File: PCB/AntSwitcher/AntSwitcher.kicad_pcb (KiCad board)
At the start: 2 copper layers, 33 parts, among them J1 Barrel_Jack, J2 TRX_UKW, J3 TRX2, J4 ANT1, J5 ANT2, K1 HF3-53, K2 HF3-53, K3 HF3-53, K4 HF3-53, Q1 Q_NMOS_GSD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

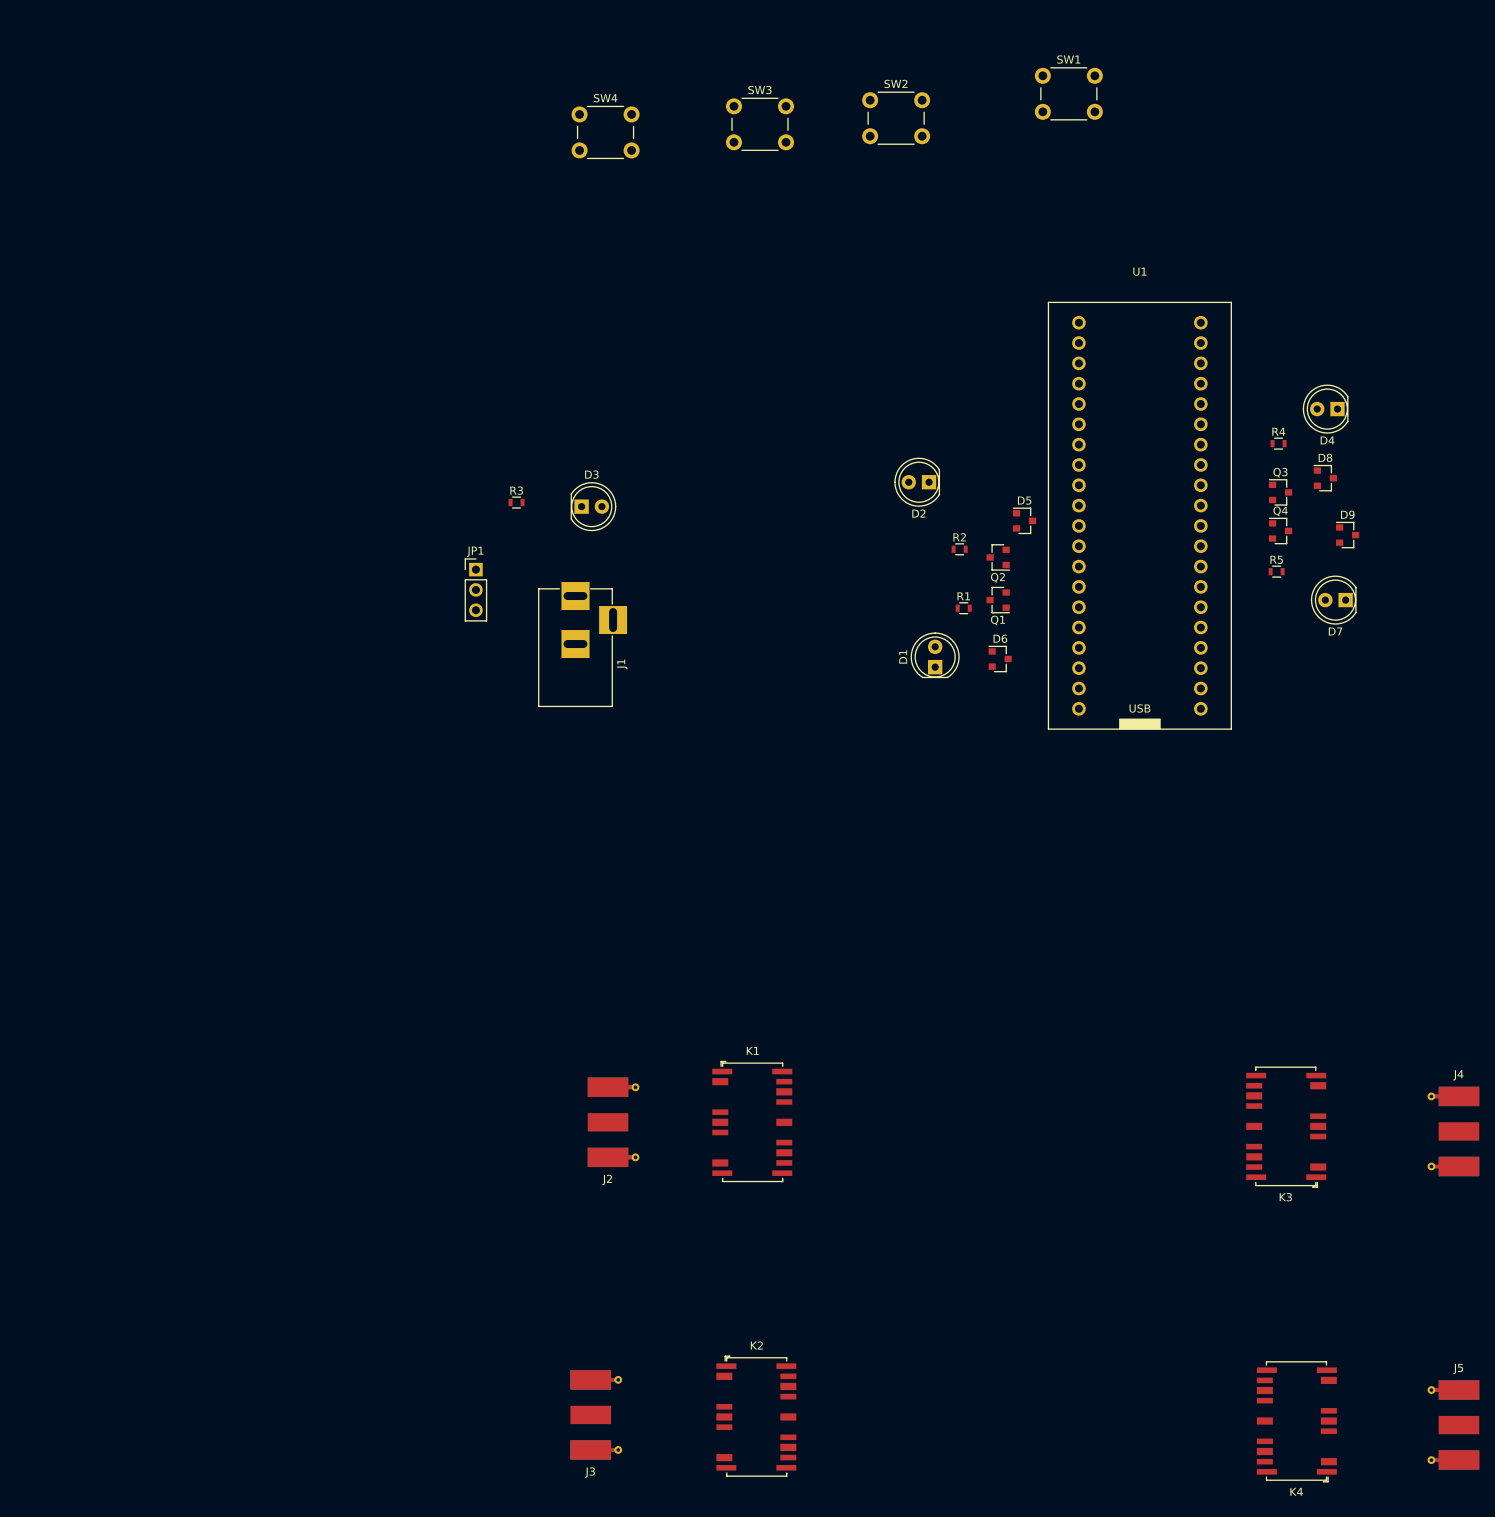
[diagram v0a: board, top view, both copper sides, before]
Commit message: HF-Layout Relays
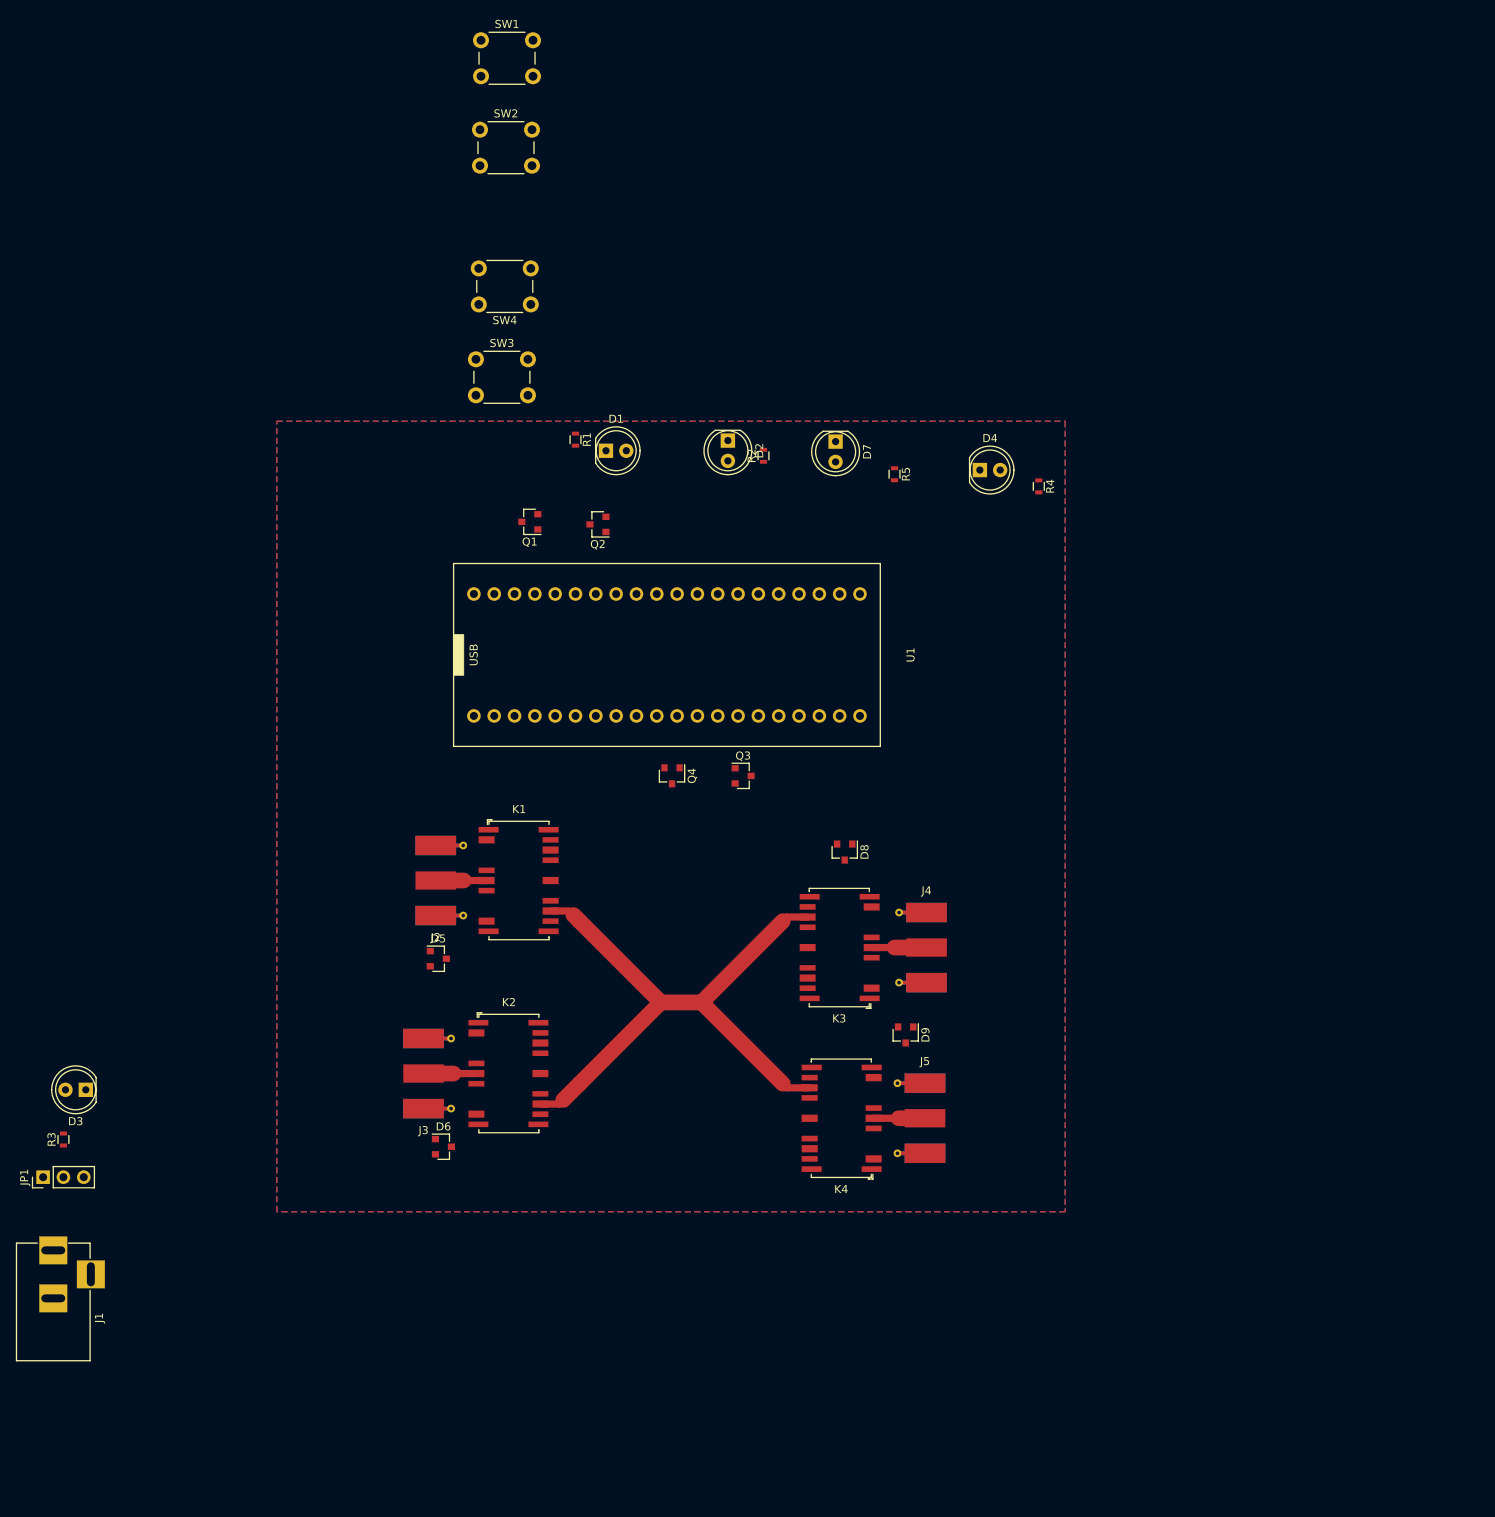
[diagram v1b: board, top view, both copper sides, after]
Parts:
- moved J1 104.6 mm to (36.3, 165.4)
- moved R3 97.7 mm to (37.6, 151.5), turned to 90 degrees
- moved D3 95.7 mm to (40.4, 145.3), turned to 180 degrees
- moved JP1 93.2 mm to (35.1, 156.2), turned to 90 degrees
- moved D6 92.5 mm to (85.1, 152.4)
- moved D5 91.5 mm to (84.5, 128.9)
- moved D9 83.4 mm to (142.9, 138.4), turned to 270 degrees
- moved Q4 82.0 mm to (113.7, 106.0), turned to 270 degrees
- moved J5 77.0 mm to (143.6, 148.8)
- moved D8 76.1 mm to (135.3, 115.6), turned to 270 degrees
- moved Q3 76.0 mm to (122.6, 106.0)
- moved J4 70.4 mm to (143.8, 127.5)
- moved SW1 70.4 mm to (89.8, 14.1)
- moved K4 68.3 mm to (134.9, 148.8)
- moved D7 66.8 mm to (134.1, 64.3), turned to 270 degrees
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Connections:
- D5 pad 1: Net-(D5-Pad1) -> GNDREF
- D5 pad 2: GNDREF -> (no net)
- D5 pad 3: (no net) -> Net-(D5-Pad3)
- D6 pad 1: Net-(D6-Pad1) -> GNDREF
- D6 pad 2: GNDREF -> (no net)
- D6 pad 3: (no net) -> Net-(D6-Pad3)
- D8 pad 1: Net-(D8-Pad1) -> GNDREF
- D8 pad 2: GNDREF -> (no net)
- D8 pad 3: (no net) -> Net-(D8-Pad3)
- D9 pad 1: Net-(D9-Pad1) -> GNDREF
- D9 pad 2: GNDREF -> (no net)
- D9 pad 3: (no net) -> Net-(D9-Pad3)
- K1 pad 11: Net-(D5-Pad1) -> Net-(D5-Pad3)
- K2 pad 11: Net-(D6-Pad1) -> Net-(D6-Pad3)
- K3 pad 11: Net-(D8-Pad1) -> Net-(D8-Pad3)
- K4 pad 11: Net-(D9-Pad1) -> Net-(D9-Pad3)
- Q1 pad 3: Net-(D6-Pad1) -> Net-(D6-Pad3)
- Q2 pad 3: Net-(D5-Pad1) -> Net-(D5-Pad3)
- Q3 pad 3: Net-(D8-Pad1) -> Net-(D8-Pad3)
- Q4 pad 3: Net-(D9-Pad1) -> Net-(D9-Pad3)
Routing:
- net Net-(K1-Pad14): track 0.00 -> 78.9 mm
- net Net-(J4-Pad1): track 0.00 -> 6.86 mm
- net Net-(J3-Pad1): track 0.00 -> 6.61 mm
- net Net-(J5-Pad1): track 0.00 -> 6.41 mm
- net Net-(J2-Pad1): track 0.00 -> 6.36 mm
- added copper zone on B.Cu, net GNDREF
- added copper zone on F.Cu, net GNDREF

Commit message: Layout components placement
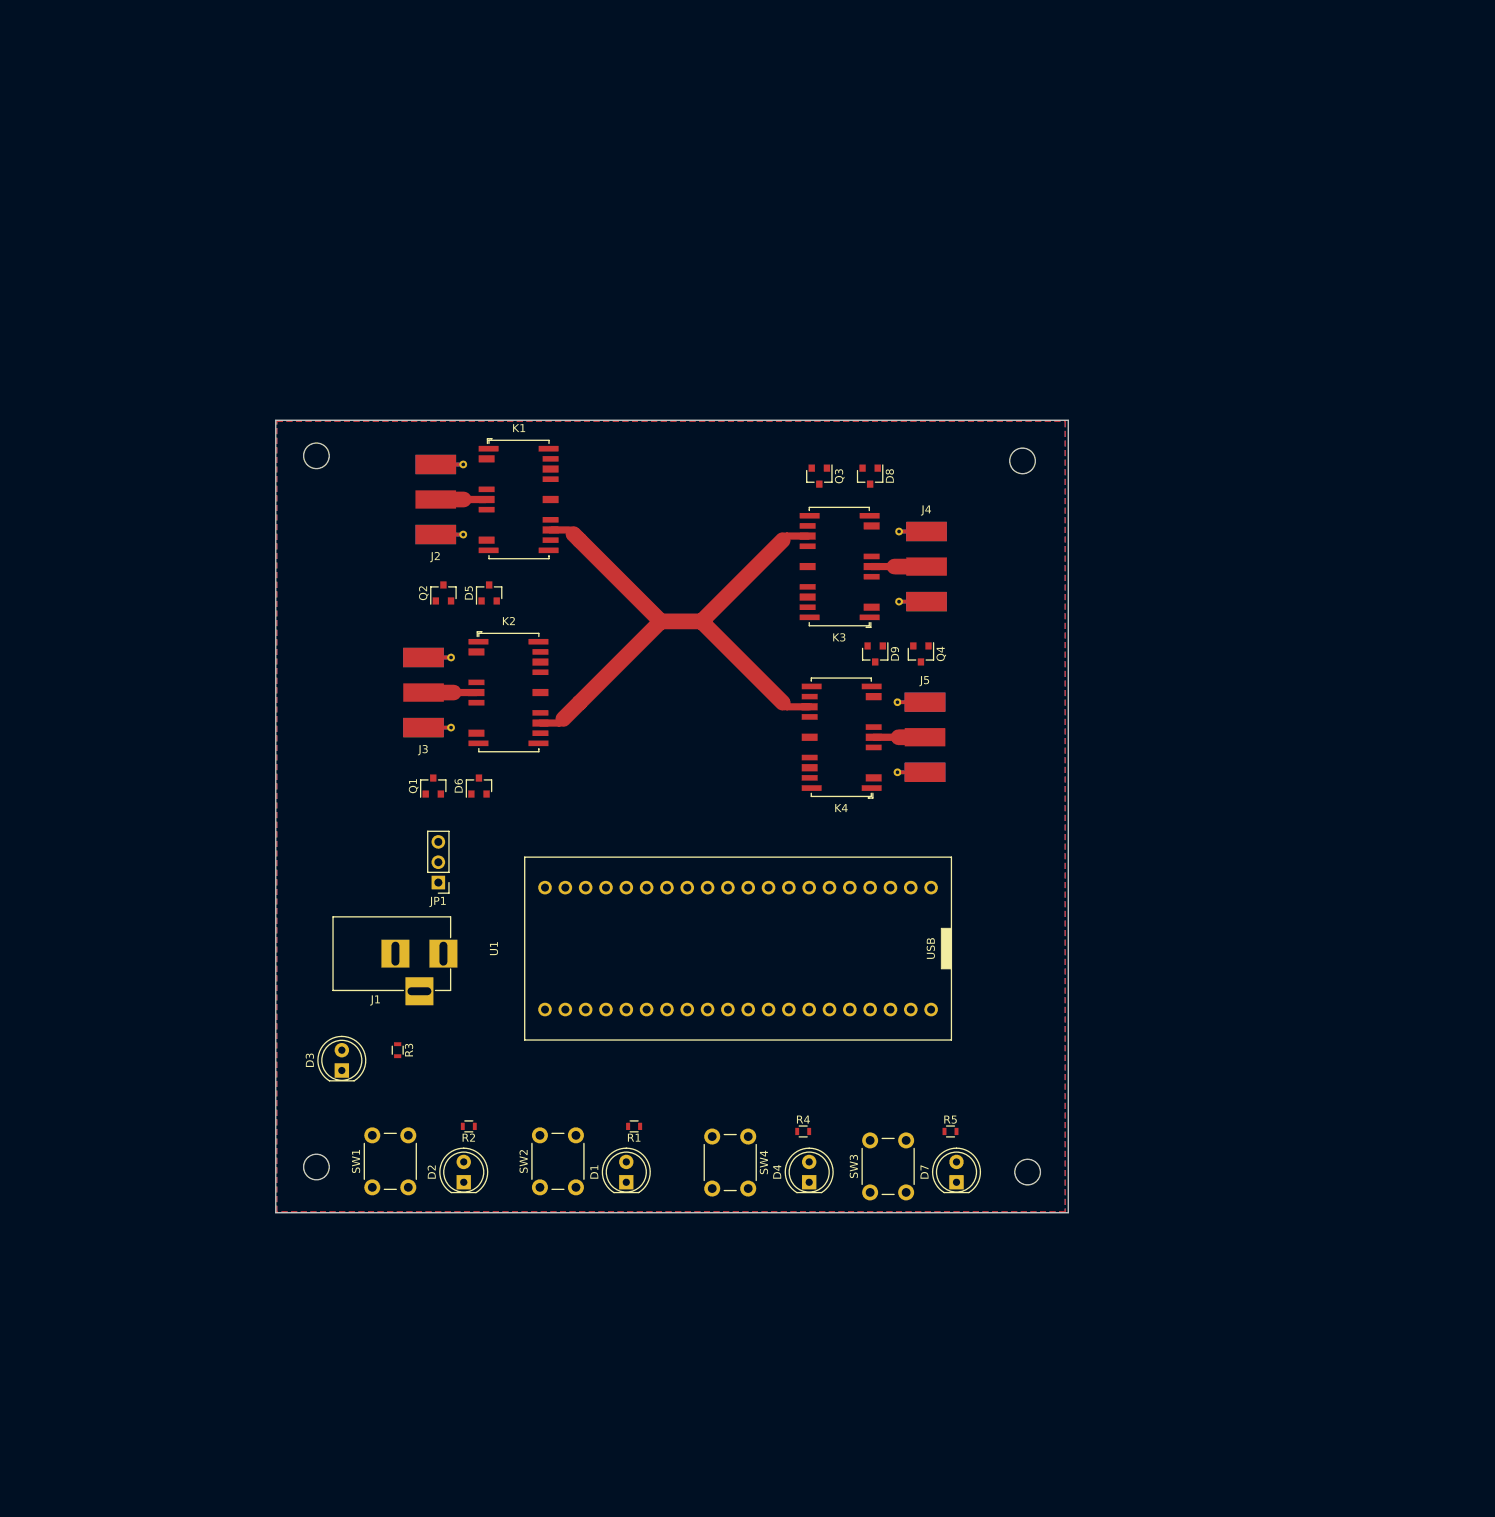
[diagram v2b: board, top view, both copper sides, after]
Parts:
- added REF**: MountingHole_3.2mm_M3, Mounting_Holes:MountingHole_3.2mm_M3, F.Cu at (69.2, 66.0)
- added REF**: MountingHole_3.2mm_M3, Mounting_Holes:MountingHole_3.2mm_M3, F.Cu at (157.5, 66.7)
- added REF**: MountingHole_3.2mm_M3, Mounting_Holes:MountingHole_3.2mm_M3, F.Cu at (158.1, 155.6)
- added REF**: MountingHole_3.2mm_M3, Mounting_Holes:MountingHole_3.2mm_M3, F.Cu at (69.2, 154.9)
- moved SW1 144.0 mm to (76.2, 157.5), turned to 90 degrees
- moved SW2 132.4 mm to (97.2, 157.5), turned to 90 degrees
- moved SW3 115.2 mm to (138.4, 158.1), turned to 90 degrees
- moved SW4 107.5 mm to (123.2, 151.1), turned to 270 degrees
- moved D2 98.4 mm to (87.6, 156.8), turned to 90 degrees
- moved D7 93.8 mm to (149.2, 156.8), turned to 90 degrees
- moved R2 91.6 mm to (88.3, 149.9), turned to 180 degrees
- moved D4 91.5 mm to (130.8, 156.8), turned to 90 degrees
- moved D1 91.5 mm to (108.0, 156.8), turned to 90 degrees
- moved R1 86.2 mm to (108.9, 149.9), turned to 180 degrees
- moved R4 85.8 mm to (130.1, 150.5), turned to 0 degrees
- moved R5 82.5 mm to (148.5, 150.5), turned to 0 degrees
- moved JP1 61.6 mm to (84.5, 119.4), turned to 180 degrees
- moved J1 61.3 mm to (85.1, 128.3), turned to 0 degrees
- moved D9 47.8 mm to (139.1, 90.8)
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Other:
- board outline added: 99.1 x 99.1 mm

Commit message: Layout Routing draft
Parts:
- moved JP1 5.72 mm to (78.7, 119.4)
- moved R1 0.98 mm to (108.0, 149.9), turned to 270 degrees
- moved R2 0.64 mm to (87.6, 149.9), turned to 270 degrees
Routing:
- net +5V: track 0.00 -> 245.5 mm, vias 0 -> 4
- net Net-(Q2-Pad1): track 0.00 -> 125.5 mm, vias 0 -> 2
- net Net-(Q1-Pad1): track 0.00 -> 86.3 mm
- net Net-(JP1-Pad3): track 0.00 -> 28.4 mm
- net GNDREF: track 0.00 -> 27.5 mm
- net Net-(SW2-Pad2): track 0.00 -> 20.9 mm, vias 0 -> 1
- net Net-(J1-Pad1): track 0.00 -> 11.5 mm
- net Net-(D2-Pad2): track 0.00 -> 3.69 mm
- net Net-(D1-Pad2): track 0.00 -> 3.69 mm

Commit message: Layout final
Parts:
- moved R3 7.00 mm to (73.1, 137.2), turned to 180 degrees
- moved R4 0.91 mm to (130.8, 150.0), turned to 270 degrees
- moved R5 0.91 mm to (149.2, 150.0), turned to 270 degrees
- moved D3 0.63 mm to (72.4, 143.5)
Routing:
- net Net-(Q3-Pad1): track 0.00 -> 189.6 mm, vias 0 -> 1
- net Net-(Q4-Pad1): track 0.00 -> 110.9 mm
- net Net-(SW1-Pad2): track 0.00 -> 44.0 mm
- net Net-(SW3-Pad2): track 0.00 -> 42.8 mm
- net Net-(SW4-Pad2): track 0.00 -> 24.7 mm
- net +5V: track 245.5 -> 267.8 mm
- net Net-(D8-Pad3): track 0.00 -> 10.3 mm
- net Net-(D5-Pad3): track 0.00 -> 10.1 mm
- net Net-(D6-Pad3): track 0.00 -> 10.1 mm
- net Net-(D9-Pad3): track 0.00 -> 8.96 mm
- net Net-(SW2-Pad2): track 20.9 -> 28.1 mm, vias 1 -> 0
- net Net-(D3-Pad2): track 0.00 -> 3.81 mm
- net Net-(D7-Pad2): track 0.00 -> 3.58 mm
- net Net-(D4-Pad2): track 0.00 -> 3.58 mm
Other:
- board text added: "ANT1"
- board text added: "ANT2"
- board text added: "Antennenschaltbox HF-Relais HF3-53 DM1JZ 2020-08"
- board text added: "TRX1"
- board text added: "TRX2"

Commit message: Barrel Jack changed to SMD variant
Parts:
- J1: footprint Connectors:BARREL_JACK -> BarrelJackSMD:BarrelJackSMD
- moved J1 4.84 mm to (80.6, 130.2)
